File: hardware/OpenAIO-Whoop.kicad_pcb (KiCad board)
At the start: 6 copper layers, 30.3 x 30.3 mm, 250 parts, among them J1 U.FL, J10 M3, J13 M4, J2 +, J20 LED, J21 5V, J22 BZ-, J23 CAM, J24 5V, J25 GND, J26 VHD, J27 GND, J28 TX0, J29 RX0, J3 -, J31 USB, J32 CAM, J33 GND, J4 M1, J7 M2, Q26 AP1606, Q27 BC857BM, Q28 AP1606, Q29 AGM210MAP, Q30 AGM210MAP, Q31 AGM210MAP, Q32 AGM210MAP, Q33 AGM210MAP, Q34 AGM210MAP, Q35 AGM210MAP, Q36 AGM210MAP, Q37 AGM210MAP, Q38 AGM210MAP, Q39 AGM210MAP, Q40 AGM210MAP, SW1 SKUBAAE010, U1 INA186A3, U10 RP2354A, U11 BMI270, U12 TPS7A2018, U13 PY25Q128HA-DFH-IR, U14 SN74LVC1G3157, U15 TLV7031, U16 ESP32-PICO-V3, U18 SX1281, U19 RTC6705, U2 TPS61022, U20 SE5004L, U21 LP5912-3.3, U22 LP5907-2.85, U4 LP5912-3.3, U6 EFM8BB51F16I, U7 EFM8BB51F16I, U8 EFM8BB51F16I, U9 EFM8BB51F16I, X1 12MHz, X3 52MHz TCXO, X4 8MHz 10pF

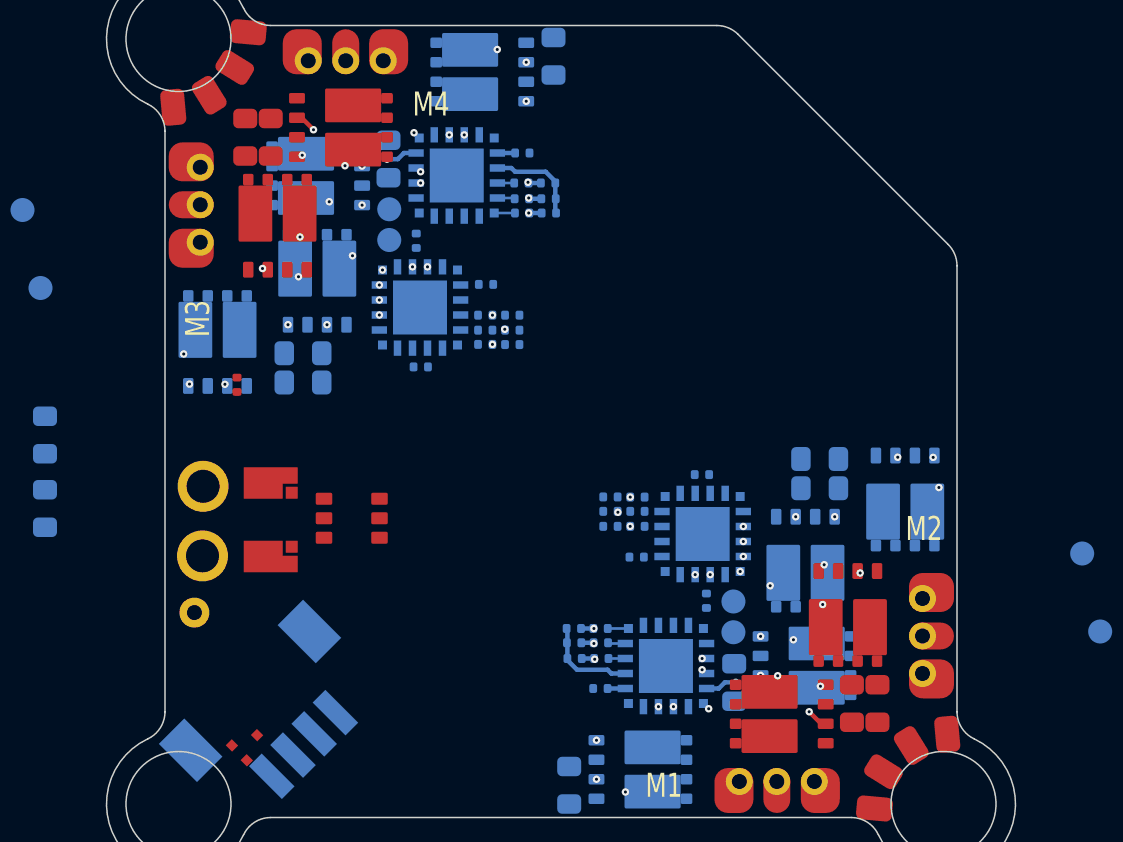
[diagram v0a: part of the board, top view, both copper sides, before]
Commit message: ESC routing back on In4 with legal 1+4+1 vias; Phase class at signal size (D121)
- Restores the owner's ESC gate and BEMF routing from 350048e on In4 (L5),
  replacing the In2 conversion and its 70 buried vias (12 remain).
- B-side ends use one L5-L6 microvia. F-side gate pads take a microvia
  L1-L2 into the pad plus a buried L2-L5 via staggered 0.25 mm. The two
  through vias become microvias.
- In4 becomes a GND pour that carries only ESC routing: DRU warning
  scoped to non-ESC nets, layer type mixed, board stackup note updated.
- Phase class drops to 0.10 / 0.09 / via 0.35 / 0.15, because phases are
  drawn as zones and the net also carries the BEMF taps.
- Removes the In2 ESC routing and the 0.40 / 0.20 buried vias on the
  PHASE nets.

Co-Authored-By: Claude Opus 5.5 <noreply@anthropic.com>
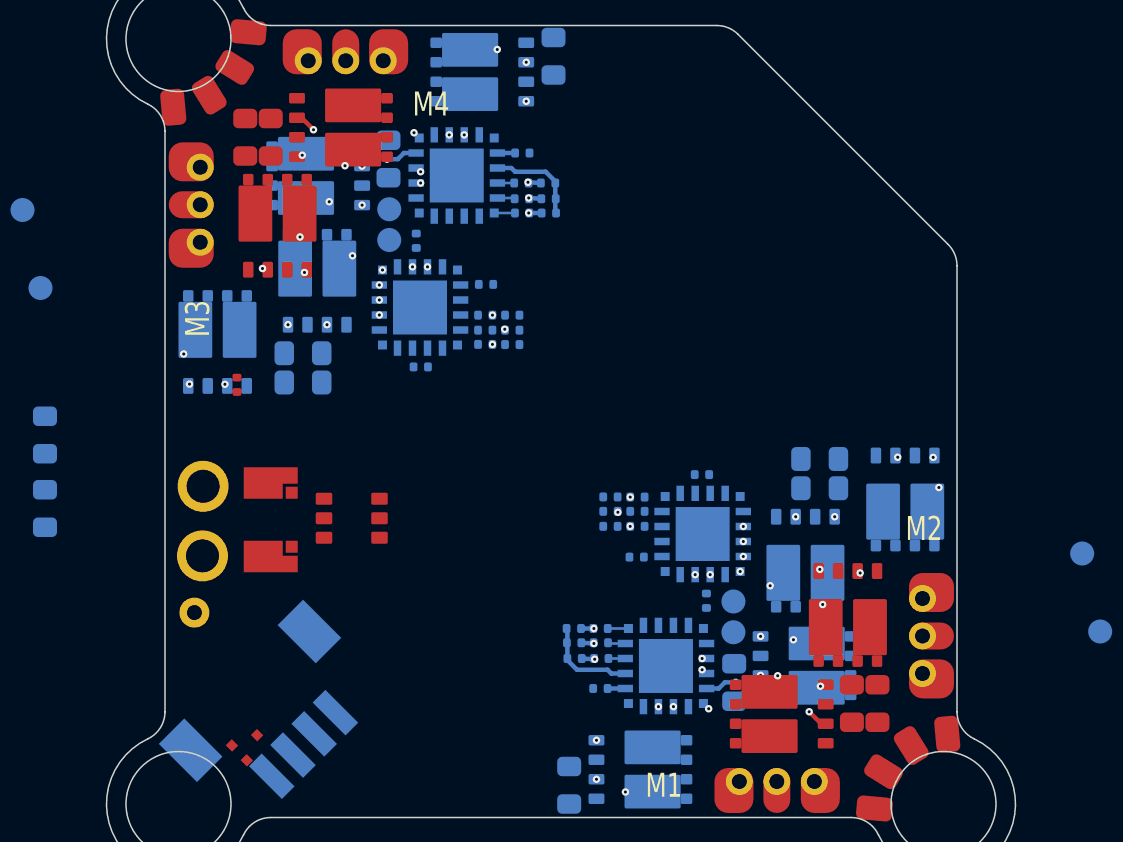
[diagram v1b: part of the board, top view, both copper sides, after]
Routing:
- net /ESC3/B_COM: track 2.31 -> 2.99 mm, vias 4 -> 3
- net /ESC2/B_COM: track 2.31 -> 2.93 mm, vias 4 -> 3
- net /ESC4/PHASE_A: track 7.22 -> 7.74 mm, vias 4 -> 2
- net /ESC1/PHASE_A: track 7.22 -> 7.74 mm, vias 4 -> 2
- net /ESC4/C_PWM: track 4.99 -> 5.49 mm, vias 4 -> 2
- net /ESC4/A_COM: track 3.64 -> 4.14 mm, vias 4 -> 2
- net /ESC3/PHASE_C: track 5.91 -> 6.41 mm, vias 4 -> 2
- net /ESC2/PHASE_C: track 5.91 -> 6.41 mm, vias 4 -> 2
- net /ESC1/C_PWM: track 4.99 -> 5.49 mm, vias 4 -> 2
- net /ESC1/A_COM: track 3.64 -> 4.14 mm, vias 4 -> 2
- net /ESC1/C_COM: track 4.15 -> 4.65 mm, vias 4 -> 2
- net /ESC4/C_COM: track 4.15 -> 4.65 mm, vias 4 -> 2
- net /ESC2/C_PWM: track 1.59 -> 2.09 mm, vias 4 -> 2
- net /ESC3/C_PWM: track 1.59 -> 2.09 mm, vias 4 -> 2
- net /ESC3/PHASE_A: track 12.5 -> 13.0 mm, vias 4 -> 2
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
